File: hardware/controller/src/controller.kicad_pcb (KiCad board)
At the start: 2 copper layers, 85 x 35 mm, 41 parts, among them J1 To Display, J2 Display, J3 Barrel_Jack_Switch, J4 Program, J5 JTAG, SW1 RESET, SW2 BTN1, SW3 BTN1, U1 ESP32-WROOM-E, U2 XL1509-5.0, U3 XL1509-3.3, U4 RS0102YH8, U5 ESP32-S3-WROOM-1

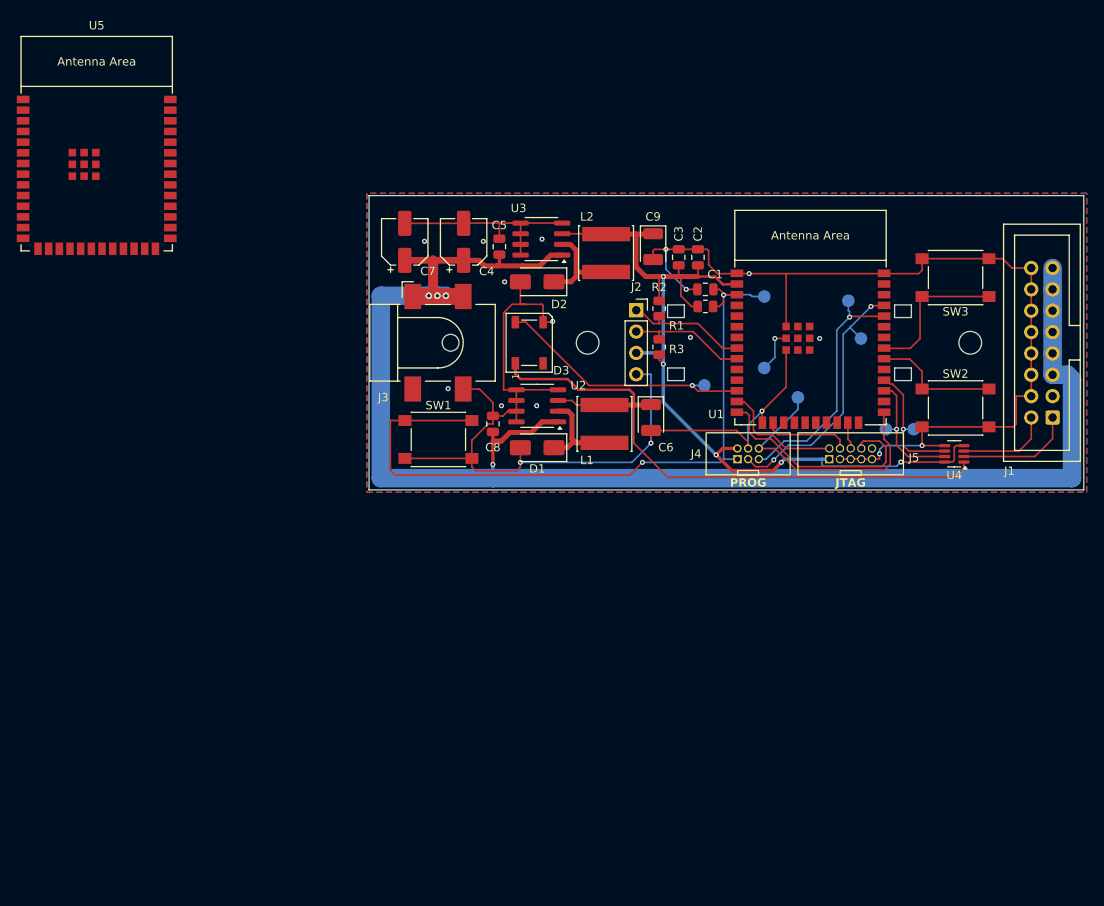
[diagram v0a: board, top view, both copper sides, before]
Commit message: Design controller as a top connector board.
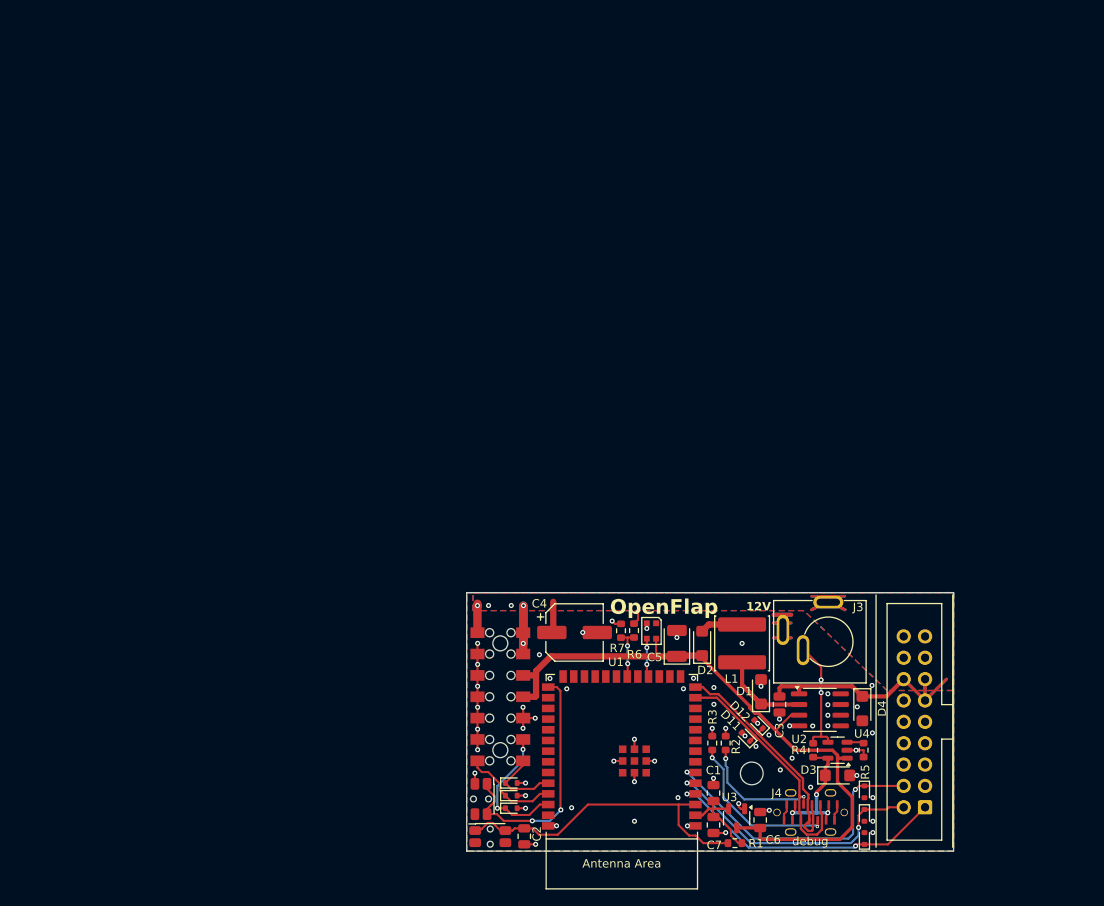
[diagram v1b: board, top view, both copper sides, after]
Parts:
- removed C8: 100nF, Capacitor_SMD:C_0805_2012Metric
- removed C9: 100uF, Capacitor_Tantalum_SMD:CP_EIA-3528-21_Kemet-B
- removed H2: MountingHole, MountingHole:MountingHole_2.7mm_M2.5
- removed J5: JTAG, BoxHeader:2x05 Box Header 1.27
- removed L2: 47uH, Inductor_SMD:L_Sunlord_SWPA6045S
- removed OSHW_LOGO_1: OSHW-Logo_5.7x6mm_SilkScreen, Symbol:OSHW-Logo_5.7x6mm_SilkScreen
- removed SW3: BTN1, Button_Switch_SMD:SW_SPST_PTS645
- removed TP1, TP2, TP3, TP4, TP5, TP6, TP7, TP8: ~, TestPoint:TestPoint_Pad_D1.5mm
- removed U5: ESP32-S3-WROOM-1, PCM_Espressif:ESP32-S3-WROOM-1
- added D10: PESD3V3, Diode_SMD:D_SOD-523, F.Cu at (91.5, 153.7)
- added D11: PESD5V0, Diode_SMD:D_SOD-523, F.Cu at (119.4, 145.2)
- added D12: PESD5V0, Diode_SMD:D_SOD-523, F.Cu at (120.9, 143.7)
- added D4: SMF12A, Diode_SMD:D_SMF, F.Cu at (133.3, 141.9)
- added D5: PESD3V3, Diode_SMD:D_SOD-523, F.Cu at (133.5, 157.3)
- added D6: PESD3V3, Diode_SMD:D_SOD-523, F.Cu at (133.5, 154.6)
- added D7: PESD3V3, Diode_SMD:D_SOD-523, F.Cu at (91.5, 150.7)
- added D8: PESD3V3, Diode_SMD:D_SOD-523, F.Cu at (91.5, 152.2)
- added D9: PESD3V3, Diode_SMD:D_SOD-523, F.Cu at (133.5, 151.8)
- added LED1: WS2812B-2020, LED_SMD:LED_WS2812B-2020_PLCC4_2.0x2.0mm, F.Cu at (108.2, 132.6)
- added R4: 10K, Resistor_SMD:R_0603_1608Metric, F.Cu at (127.4, 146.8)
- added R5: 10K, Resistor_SMD:R_0603_1608Metric, F.Cu at (133.4, 146.8)
- added R6: 220K, Resistor_SMD:R_0603_1608Metric, F.Cu at (106.1, 132.6)
- added R7: 20K, Resistor_SMD:R_0603_1608Metric, F.Cu at (104.6, 132.6)
- C2: value 10uF -> 100nF
- C4: value 22uF -> 220uF; footprint Capacitor_SMD:CP_Elec_5x5.4 -> Capacitor_SMD:CP_Elec_6.3x7.7
- C5: value 100nF -> 100uF; footprint Capacitor_SMD:C_0805_2012Metric -> Capacitor_Tantalum_SMD:CP_EIA-3528-21_Kemet-B
- C6: value 100uF -> 10uF; footprint Capacitor_Tantalum_SMD:CP_EIA-3528-21_Kemet-B -> Capacitor_SMD:C_0805_2012Metric
- C7: value 22uF -> 10uF; footprint Capacitor_SMD:CP_Elec_5x5.4 -> Capacitor_SMD:C_0805_2012Metric
- D1, D2: value SS210 -> K24; footprint Diode_SMD:D_SMA -> Diode_SMD:D_SMF
- D3: value WS2812B -> SMF5V0A; footprint LED_SMD:LED_WS2812B_PLCC4_5.0x5.0mm_P3.2mm -> Diode_SMD:D_SMF
- J1: value To Display -> Column Connector; footprint Connector_IDC:IDC-Header_2x08_P2.54mm_Vertical -> Connector_Samtec_HLE_SMD:Samtec_HLE-107-02-xxx-DV-BE-A_2x07_P2.54mm_Horizontal
- J2: value Display -> Row Connector; footprint Connector_PinSocket_2.54mm:PinSocket_1x04_P2.54mm_Vertical -> Connector_IDC:IDC-Header_2x09_P2.54mm_Vertical
- J3: value Barrel_Jack_Switch -> 12V DC Barrel Jack; footprint Connector_BarrelJack:BarrelJack_CLIFF_FC681465S_SMT_Horizontal -> DC-jack-connector:DC-012A-25A
- J4: value Program -> USB C; footprint BoxHeader:2x03 Box Header 1.27 -> USB-C-connector:MC-803LS-HXXX
- R1: footprint Resistor_SMD:R_0805_2012Metric -> Resistor_SMD:R_0603_1608Metric
- R2, R3: value 10K -> 5K1; footprint Resistor_SMD:R_0805_2012Metric -> Resistor_SMD:R_0603_1608Metric
- SW1: footprint Button_Switch_SMD:SW_SPST_PTS645 -> Button_Switch_SMD:SW_SPST_EVQP7C
- SW2: value BTN1 -> BOOT; footprint Button_Switch_SMD:SW_SPST_PTS645 -> Button_Switch_SMD:SW_SPST_EVQP7C
- U1: value ESP32-WROOM-E -> ESP32-S3-WROOM-1; footprint PCM_Espressif:ESP32-WROOM-32E -> PCM_Espressif:ESP32-S3-WROOM-1
- U3: value XL1509-3.3 -> XC6206P332MR; footprint Package_SO:SOIC-8_3.9x4.9mm_P1.27mm -> Package_TO_SOT_SMD:SOT-23-3
- U4: value RS0102YH8 -> MT9700; footprint Package_TO_SOT_SMD:SOT-23-8 -> Package_TO_SOT_SMD:SOT-23-5
- moved C7 78.5 mm to (115.6, 155.7), turned to -90 degrees
- moved J1 73.6 mm to (90.2, 140.4), turned to 90 degrees
- moved SW2 73.1 mm to (87.9, 152.6), turned to -90 degrees
- moved U3 72.7 mm to (118.3, 154.9), turned to -90 degrees
- moved C2 71.9 mm to (93.1, 157.0)
- moved J2 68.4 mm to (140.7, 153.6), turned to 180 degrees
- moved R1 63.9 mm to (118.1, 157.9), turned to 0 degrees
- moved D3 63.2 mm to (130.3, 149.8), turned to 0 degrees
- moved C1 59.9 mm to (115.6, 151.9), turned to 90 degrees
- moved J3 58.5 mm to (129.2, 133.9), turned to -90 degrees
- moved U1 55.2 mm to (104.7, 147.5), turned to 180 degrees
- moved H1 54.8 mm to (120.1, 149.6)
- moved C3 54.5 mm to (123.4, 141.4), turned to -90 degrees
- moved R2 52.3 mm to (117.0, 146.0), turned to 90 degrees
- moved C5 51.7 mm to (111.2, 134.1)
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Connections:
- C1 pad 1: GND -> +3V3
- C1 pad 2: /EN -> GND
- C2 pad 1: +3V3 -> GND
- C2 pad 2: GND -> /EN
- C3 pad 1: +3V3 -> +12V
- C5 pad 1: +12V -> +5V
- C7 pad 1: +12V -> +3V3
- D2 pad 1: Net-(D2-K) -> +5V
- D2 pad 2: GND -> Net-(D2-A)
- D3 pad 1: +5V -> VBUS
- D3 pad 2: unconnected-(D3-DOUT-Pad2) -> GND
- J1 pad 1: /UART1_RX_M -> /UART0_RX_B
- J1 pad 14: GND -> +12V
- J1 pad 2: /UART1_TX_M -> /UART0_TX_B
- J1 pad 3: unconnected-(J1-Pin_3-Pad3) -> /COL END
- J1 pad 5: +12V -> GND
- J1 pad 7: +12V -> +5V
- J1 pad 9: +12V -> +5V
- J2 pad 1: /SDA -> /UART0_RX_A
- J2 pad 2: /SCL -> /UART0_TX_A
- J2 pad 3: +3V3 -> GND
- J2 pad 4: GND -> /ROW END
- J3 pad 3: GND -> /DC_JACK_SW
- L1 pad 2: +5V -> Net-(D2-A)
- R2 pad 1: +3V3 -> Net-(J4-CC1)
- R2 pad 2: /SDA -> GND
- R3 pad 1: +3V3 -> Net-(J4-CC2)
- R3 pad 2: /SCL -> GND
- SW2 pad 1: /BTN1 -> /IO0
- U1 pad 12: /WLED -> unconnected-(U1-GPIO8/TOUCH8/ADC1_CH7/SUBSPICS1-Pad12)
- U1 pad 13: /TMS -> /USB_D-
- U1 pad 14: /TDI -> /USB_D+
- U1 pad 15: GND -> unconnected-(U1-GPIO3/TOUCH3/ADC1_CH2-Pad15)
- U1 pad 16: /TCK -> unconnected-(U1-GPIO46-Pad16)
- U1 pad 17: (no net) -> unconnected-(U1-GPIO9/TOUCH9/ADC1_CH8/FSPIHD/SUBSPIHD-Pad17)
- U1 pad 18: (no net) -> /DLED
- U1 pad 19: (no net) -> unconnected-(U1-GPIO11/TOUCH11/ADC2_CH0/FSPID/FSPIIO5/SUBSPID-Pad19)
- U1 pad 20: (no net) -> /12V OK
- U1 pad 21: (no net) -> unconnected-(U1-GPIO13/TOUCH13/ADC2_CH2/FSPIQ/FSPIIO7/SUBSPIQ-Pad21)
- U1 pad 22: (no net) -> unconnected-(U1-GPIO14/TOUCH14/ADC2_CH3/FSPIWP/FSPIDQS/SUBSPIWP-Pad22)
- U1 pad 23: /TDO -> unconnected-(U1-GPIO21-Pad23)
- U1 pad 25: /IO0 -> unconnected-(U1-GPIO48/SPICLK_N/SUBSPICLK_N_DIFF-Pad25)
- U1 pad 27: /UART1_RX -> /IO0
- U1 pad 28: /UART1_TX -> unconnected-(U1-SPIIO6/GPIO35/FSPID/SUBSPID-Pad28)
- U1 pad 30: /BTN1 -> unconnected-(U1-SPIDQS/GPIO37/FSPIQ/SUBSPIQ-Pad30)
- U1 pad 31: /BTN2 -> unconnected-(U1-GPIO38/FSPIWP/SUBSPIWP-Pad31)
- U1 pad 32: (no net) -> unconnected-(U1-MTCK/GPIO39/CLK_OUT3/SUBSPICS1-Pad32)
- U1 pad 34: /UART0_RX -> unconnected-(U1-MTDI/GPIO41/CLK_OUT1-Pad34)
- U1 pad 35: /UART0_TX -> unconnected-(U1-MTMS/GPIO42-Pad35)
- U1 pad 36: unconnected-(U1-GPIO22-Pad36) -> /UART0_RX_B
- U1 pad 37: unconnected-(U1-GPIO23-Pad37) -> /UART0_TX_B
- U1 pad 38: GND -> /COL END
- U1 pad 39: GND -> unconnected-(U1-GPIO1/TOUCH1/ADC1_CH0-Pad39)
- U1 pad 4: unconnected-(U1-SENSOR_VP/GPIO36/ADC1_CH0-Pad4) -> /UART0_RX_A
- U1 pad 5: unconnected-(U1-SENSOR_VN/GPIO39/ADC1_CH3-Pad5) -> /UART0_TX_A
- U1 pad 6: unconnected-(U1-GPIO34/ADC1_CH6-Pad6) -> /ROW END
- U1 pad 8: /SDA -> unconnected-(U1-GPIO15/U0RTS/ADC2_CH4/XTAL_32K_P-Pad8)
- U1 pad 9: /SCL -> unconnected-(U1-GPIO16/U0CTS/ADC2_CH5/XTAL_32K_N-Pad9)
- U3 pad 1: +12V -> GND
- U3 pad 2: Net-(D2-K) -> +3V3
- U3 pad 3: +3V3 -> +5V
- U4 pad 2: /UART1_RX_M -> GND
- U4 pad 3: /UART1_TX_M -> Net-(U4-SET)
- U4 pad 4: +3V3 -> /DC_JACK_SW
- U4 pad 5: GND -> VBUS
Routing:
- net GND: track 261.5 -> 51.2 mm, vias 19 -> 64
- net +12V: track 184.1 -> 33.2 mm, vias 4 -> 5
- net +3V3: track 103.9 -> 11.3 mm, vias 5 -> 0
- net /EN: track 88.2 -> 38.1 mm, vias 2 -> 0
- net /ROW END: track 0.00 -> 35.2 mm, vias 0 -> 2
- net /UART0_RX_A: track 0.00 -> 33.9 mm, vias 0 -> 2
- net /UART0_TX_A: track 0.00 -> 32.9 mm, vias 0 -> 2
- net /UART0_TX: track 31.8 -> 0.00 mm, vias 2 -> 0
- net /WLED: track 31.2 -> 0.00 mm, vias 1 -> 0
- net /UART0_RX: track 29.7 -> 0.00 mm, vias 1 -> 0
- net /USB_D-: track 0.00 -> 29.2 mm
- net /USB_D+: track 0.00 -> 28.9 mm
- net /TDI: track 27.9 -> 0.00 mm
- net Net-(J4-CC2): track 0.00 -> 19.7 mm, vias 0 -> 2
- net /BTN2: track 17.7 -> 0.00 mm
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- added copper zone on B.Cu, net +12V
- added copper zone on F.Cu, net +12V
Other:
- board size 85 x 35 mm -> 57.9 x 30.7 mm
- board text added: "RST"
- board text added: "debug"
- board text removed: "${TITLE}"
- board text removed: "3V3"
- board text removed: "DISPLAY"
- board text removed: "EN"
- board text removed: "GND"
- board text removed: "JTAG"
- board text removed: "PROG"
- board text removed: "RX"
- board text removed: "SCL"
- board text removed: "SDA"
- board text removed: "TX"

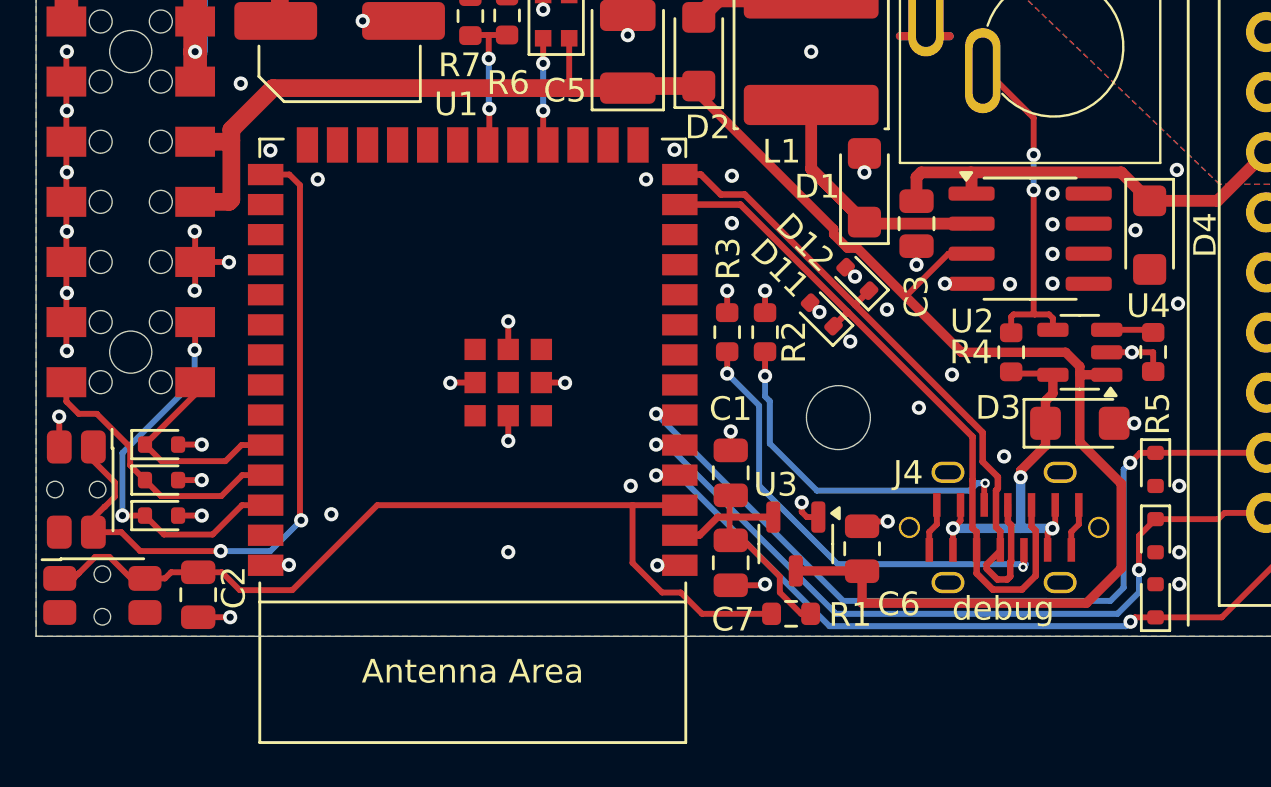
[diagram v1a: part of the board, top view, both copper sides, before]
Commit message: Add dynamic uart routing and bridging to controller, Remove OLED libs
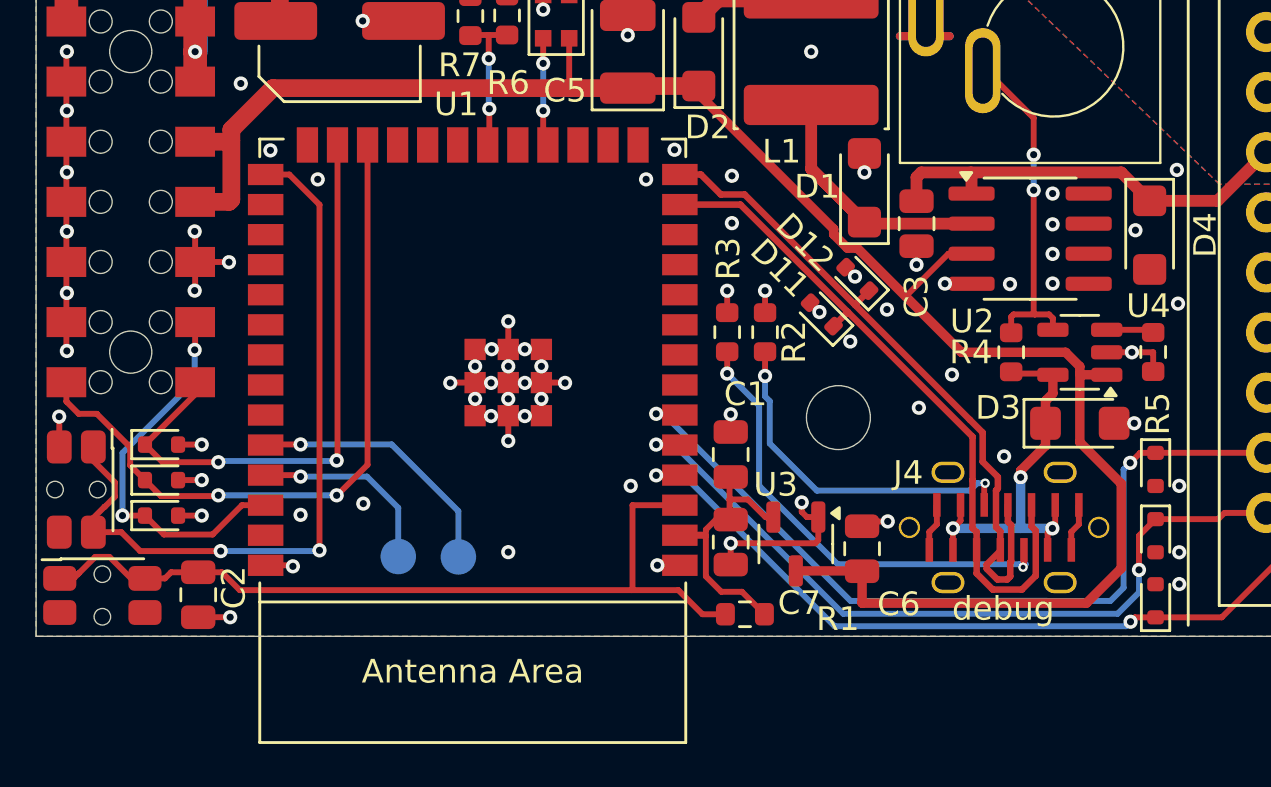
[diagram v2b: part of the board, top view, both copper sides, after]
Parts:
- added RX0: TestPoint, TestPoint:TestPoint_Pad_D1.5mm, B.Cu at (104.0, 155.4)
- added TX0: TestPoint, TestPoint:TestPoint_Pad_D1.5mm, B.Cu at (101.5, 155.4)
- moved R1 1.95 mm to (116.2, 157.9)
- moved C7 0.88 mm to (115.6, 154.8)
- moved C1 0.78 mm to (115.6, 151.1)
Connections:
- net /COL END renamed /COL START
- net /ROW END renamed /ROW START
- net /UART0_RX_A renamed /UART1_RX_A
- net /UART0_TX_A renamed /UART1_TX_A
- D7 pad 1: /UART0_RX_B -> /UART1_RX_B
- D8 pad 1: /UART0_TX_B -> /UART1_TX_B
- J1 pad 1: /UART0_RX_B -> /UART1_RX_B
- J1 pad 2: /UART0_TX_B -> /UART1_TX_B
- U1 pad 24: unconnected-(U1-GPIO47/SPICLK_P/SUBSPICLK_P_DIFF-Pad24) -> /UART1_TX_B
- U1 pad 25: unconnected-(U1-GPIO48/SPICLK_N/SUBSPICLK_N_DIFF-Pad25) -> /UART1_RX_B
- U1 pad 36: /UART0_RX_B -> /UART0_RX
- U1 pad 37: /UART0_TX_B -> /UART0_TX
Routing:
- net /UART1_TX_B: track 0.00 -> 29.7 mm, vias 0 -> 2
- net /UART1_RX_B: track 0.00 -> 25.4 mm, vias 0 -> 2
- net /UART0_TX_B: track 11.7 -> 0.00 mm
- net /UART0_RX: track 0.00 -> 11.3 mm, vias 0 -> 1
- net /UART0_RX_B: track 9.19 -> 0.00 mm
- net /UART0_TX: track 0.00 -> 8.25 mm, vias 0 -> 1
- net GND: track 51.2 -> 55.5 mm, vias 64 -> 77
- net /EN: track 38.1 -> 35.3 mm
- net /IO0: track 29.8 -> 31.7 mm
